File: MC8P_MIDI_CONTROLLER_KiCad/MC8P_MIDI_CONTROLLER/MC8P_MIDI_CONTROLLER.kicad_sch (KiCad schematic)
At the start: 29 parts, among them J1 MIDI OUT, SW1 ASSIGN, SW2 ENTER, SW3 PREV, SW4 NEXT, U1 Teensy4.0

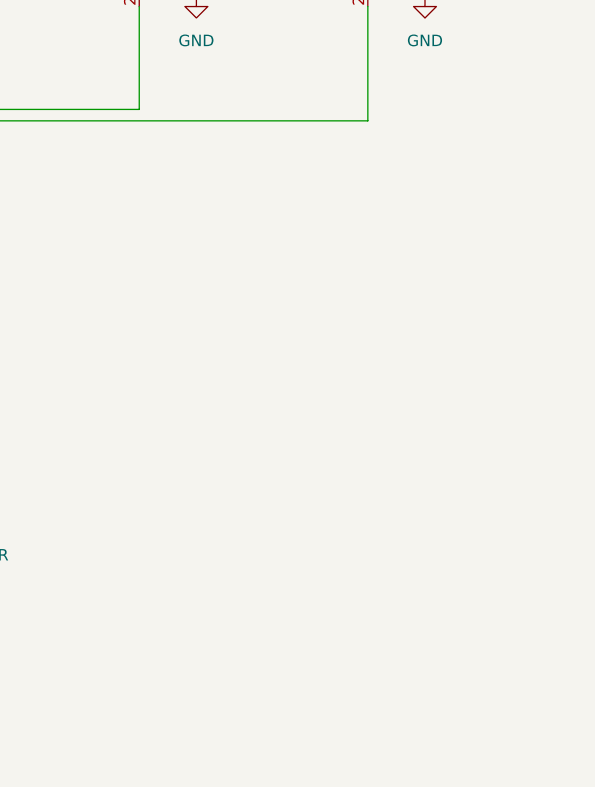
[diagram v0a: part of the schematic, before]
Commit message: Schematic update v1.2.0
- Added Bulk capacitors between the  5V and 3V3 power rails to ground for power stabilisation
- Added Decoupling capacitor between the power rails and ground for high frequency noise filtering
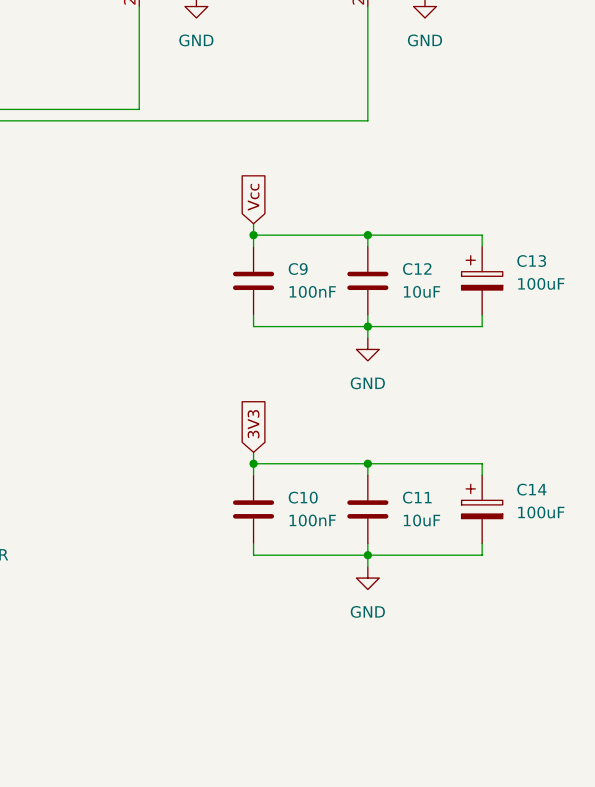
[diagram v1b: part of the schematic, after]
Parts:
- added C10, C9: 100nF, Capacitor_THT:C_Disc_D5.0mm_W2.5mm_P5.00mm, symbol Device:C
- added C11, C12: 10uF, Capacitor_THT:C_Disc_D5.0mm_W2.5mm_P5.00mm, symbol Device:C
- added C13, C14: 100uF, Capacitor_THT:CP_Radial_D4.0mm_P1.50mm, symbol Device:C_Polarized
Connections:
- net 3V3: now also C10.1, C11.1, C14.1
- net GND: now also C10.2, C11.2, C12.2, C13.2, C14.2, C9.2
- net Vcc: now also C12.1, C13.1, C9.1
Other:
- company: (none) -> .axs instruments
- title: (none) -> MC8P MIDI Controller

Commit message: PCB Update
- Fixes power resets/brownouts
- disconnected POTS, BUTTONS and MIDI OUT from Vin
- connected POTS & BUTTONS to 3V3
- connected MIDI OUT to VUSB
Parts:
- removed C10: 100nF, Capacitor_THT:C_Disc_D5.0mm_W2.5mm_P5.00mm, symbol Device:C
- removed C11: 10uF, Capacitor_THT:C_Disc_D5.0mm_W2.5mm_P5.00mm, symbol Device:C
- removed C14: 100uF, Capacitor_THT:CP_Radial_D4.0mm_P1.50mm, symbol Device:C_Polarized
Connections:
- net 3V3: now also C12.1, C13.1, C9.1, RV1.3, RV2.3, RV3.3, RV4.3, RV5.3, RV6.3, RV7.3, RV8.3, SW1.1 (A), SW2.1 (A), SW3.1 (A), SW4.1 (A)
- net Vcc: now also U1.34 (VUSB); no longer C12.1, C13.1, C9.1, RV1.3, RV2.3, RV3.3, RV4.3, RV5.3, RV6.3, RV7.3, RV8.3, SW1.1 (A), SW2.1 (A), SW3.1 (A), SW4.1 (A), U1.33 (VIN)
- no-connect marks 0 -> 33

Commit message: Schematic & PCB labelling update
Updated Capacitor labelling (C9-11)
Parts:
- renumbered C12 to C10, C13 to C11
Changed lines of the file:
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@@
 		(dnp no)
 		(fields_autoplaced yes)
-		(property "Reference" "C12"
+		(property "Reference" "C10"
 			(at 232.41 109.2199 0)
 			(effects
@@
 			(project "MC8P_MIDI_CONTROLLER"
 				(path "/42d00d8e-48e3-47e6-b456-ac5bd2d9bc78"
-					(reference "C12")
+					(reference "C10")
 					(unit 1)
 				)
@@
 		(dnp no)
 		(fields_autoplaced yes)
-		(property "Reference" "C13"
+		(property "Reference" "C11"
 			(at 245.11 108.3309 0)
 			(effects
@@
 			(project ""
 				(path "/42d00d8e-48e3-47e6-b456-ac5bd2d9bc78"
-					(reference "C13")
-					(unit 1)
-				)
+					(reference "C11")
+					(unit 1)
+				)

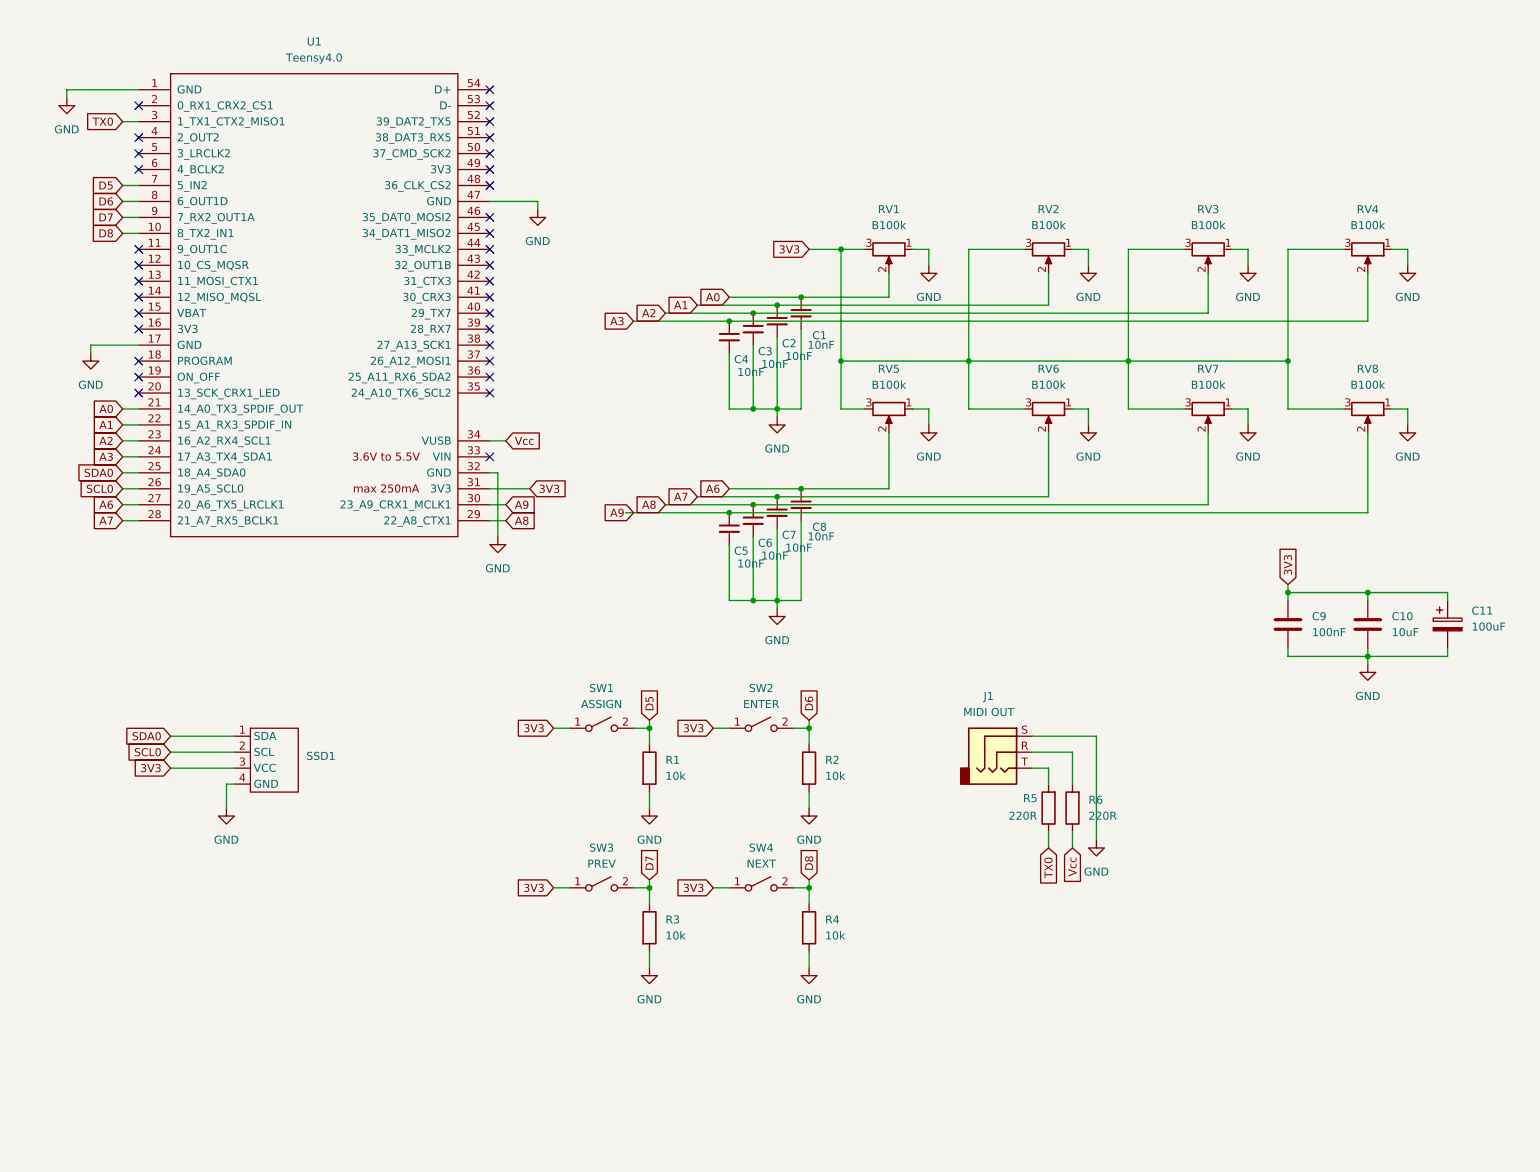
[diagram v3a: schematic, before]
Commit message: PCB Updates
- Added dedicated 5V Centre Positive power input
- Added PCBWay logo for sponsor
- Updated UI Components with new Alagard font
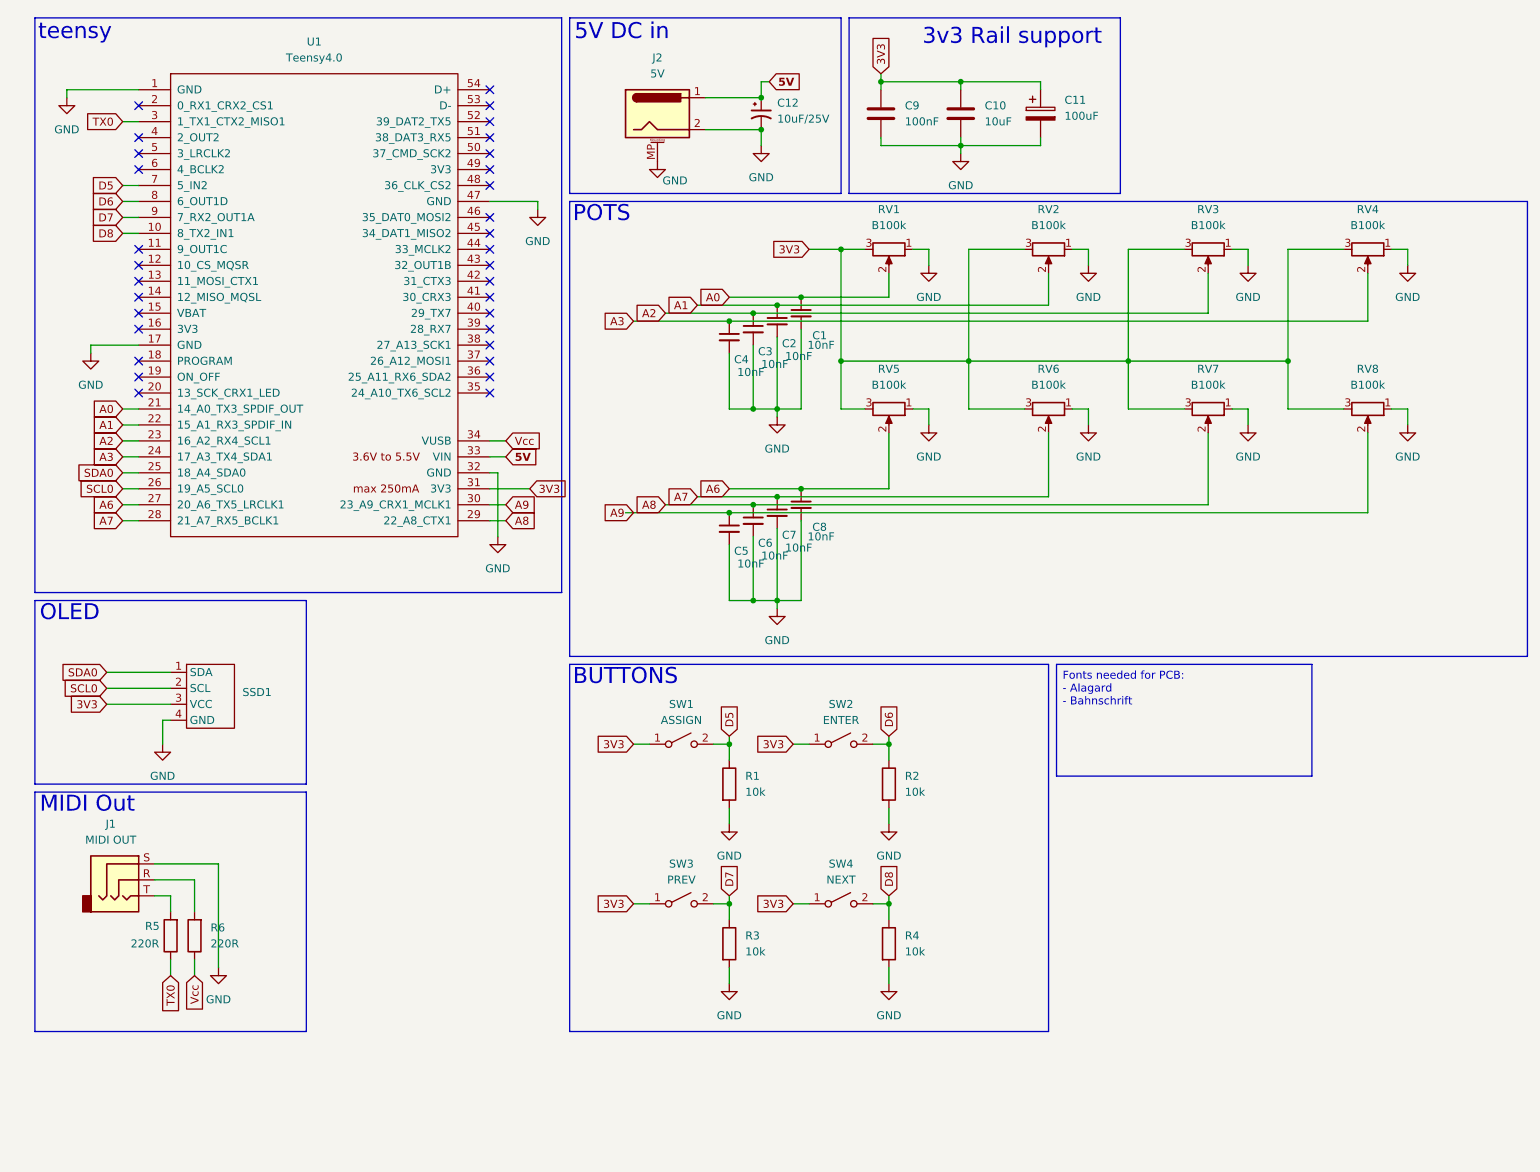
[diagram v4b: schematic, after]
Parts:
- added C12: 10uF_4x5.3_10V, Capacitor_THT:CP_Radial_D4.0mm_P1.50mm, symbol PCM_4ms_Capacitor:10uF_4x5.3_10V
- added J2: 5V, Connector_BarrelJack:BarrelJack_GCT_DCJ200-10-A_Horizontal, symbol Connector:Barrel_Jack_MountingPin
- R1, R2, R3, R4: value 10k_0402 -> 10k
- R5, R6: value 10k_0402 -> 220R
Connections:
- net GND: now also C12.2, J2.2, J2.MP (MountPin)
- net 5V: now reaches U1.33 (VIN)
- net 5V: now also C12.1, J2.1
- no-connect marks 33 -> 32
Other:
- note added: "3v3 Rail support"
- note added: "5V DC in"
- note added: "BUTTONS"
- note added: "MIDI Out"
- note added: "OLED"
- note added: "POTS"
- note added: "teensy"
- moved on the sheet: C10, C11, C9, J1, R1, R2, R3, R4, R5, R6, SSD1, SW1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

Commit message: PCB Rev3
- STM32F411CEU6 Black Pill with
W25Q64 flash
- Added DC Jack for powering externally
- restructured KiCad Folder
- Added production folder with BOM
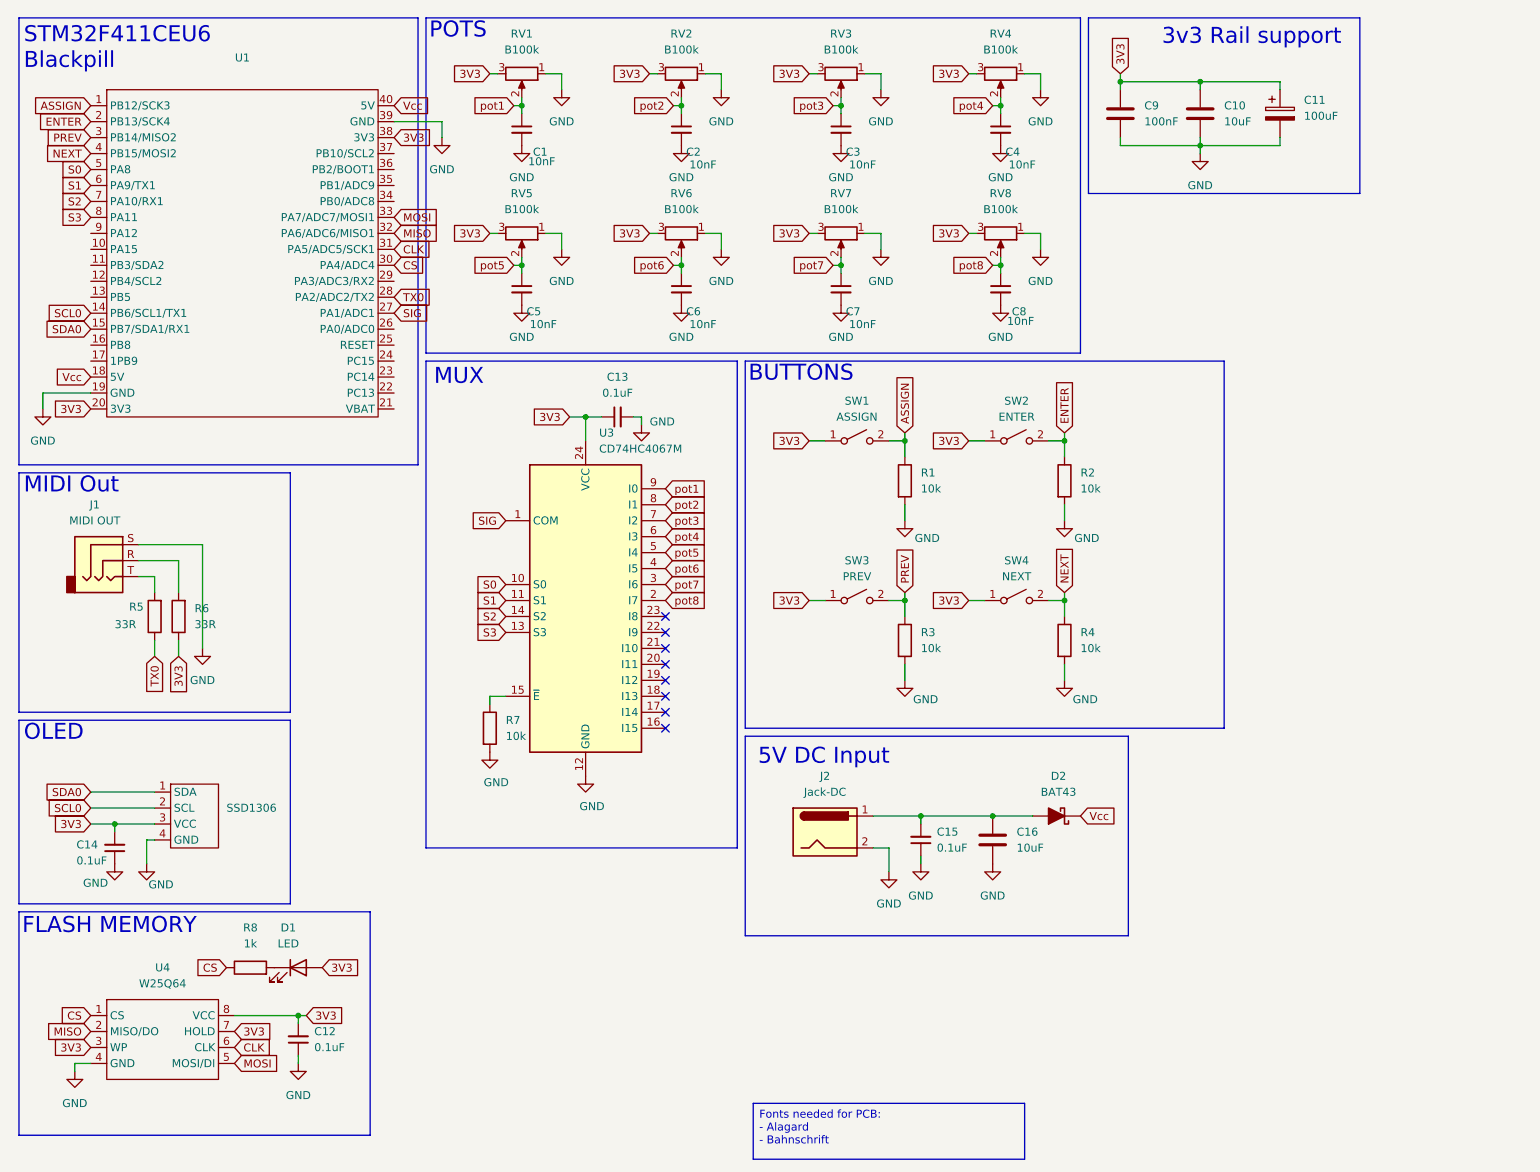
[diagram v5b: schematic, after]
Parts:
- removed C12: 10uF_4x5.3_10V, Capacitor_THT:CP_Radial_D4.0mm_P1.50mm, symbol PCM_4ms_Capacitor:10uF_4x5.3_10V
- removed J2: 5V, Connector_BarrelJack:BarrelJack_GCT_DCJ200-10-A_Horizontal, symbol Connector:Barrel_Jack_MountingPin
- removed U1: Teensy4.0, teensy:Teensy40, symbol teensy:Teensy4.0
- added C12, C13, C14, C15: 100nF_0603_16V, Capacitor_SMD:C_1206_3216Metric, symbol PCM_4ms_Capacitor:100nF_0603_16V
- added C16: 10uF, Capacitor_SMD:C_1206_3216Metric_Pad1.33x1.80mm_HandSolder, symbol Device:C
- added D1: LED, LED_SMD:LED_1206_3216Metric_Pad1.42x1.75mm_HandSolder, symbol Device:LED
- added D2: BAT43, PCM_Diode_SMD_AKL:D_1206_3216Metric_Pad1.42x1.75mm_HandSolder, symbol PCM_Diode_Schottky_AKL:BAT43
- added J2: Jack-DC, Connector_BarrelJack:BarrelJack_GCT_DCJ200-10-A_Horizontal, symbol Connector:Jack-DC
- added R7, R8: 10k_0402, PCM_4ms_Resistor:R_0603, symbol PCM_4ms_Resistor:10k_0402
- added U1: ~, blackpill:Z_module_black_pill_STM32F411, symbol STM32F411CEU6_BlackPill:BlackPill_STM32F411CEU6
- added U3: CD74HC4067M, Package_SO:SOIC-24W_7.5x15.4mm_P1.27mm, symbol 74xx:CD74HC4067M
- added U4: W25Q64, Package_SO:SOIC-8_3.9x4.9mm_P1.27mm, symbol W25Q64_SPI_FLASH:W25Q64
- C1, C2, C3, C4, C5, C6, C7, C8: footprint Capacitor_THT:C_Axial_L3.8mm_D2.6mm_P7.50mm_Horizontal -> Capacitor_SMD:C_1206_3216Metric_Pad1.33x1.80mm_HandSolder
- C10, C9: footprint Capacitor_THT:C_Disc_D5.0mm_W2.5mm_P5.00mm -> Capacitor_SMD:C_1206_3216Metric_Pad1.33x1.80mm_HandSolder
- R1, R2, R3, R4: footprint PCM_4ms_Resistor:R_Axial_DIN0207_L6.3mm_D2.5mm_P7.62mm_Horizontal -> PCM_4ms_Resistor:R_0603
- R5, R6: footprint PCM_4ms_Resistor:R_Axial_DIN0207_L6.3mm_D2.5mm_P7.62mm_Horizontal -> PCM_4ms_Resistor:R_0603; Display 220R -> 33R
- renumbered SSD1 to SSD1306
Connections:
- net 3V3: now also R6.1, C12.2, C13.1, C14.2, D1.2 (A), U1.20 (3V3), U1.38 (3V3), U3.24 (VCC), U4.3 (WP), U4.7 (HOLD), U4.8 (VCC)
- net GND: now also C12.1, C13.2, C14.1, C15.1, C16.2, J2.2, R7.2, U1.19 (GND), U1.39 (GND), U3.12 (GND), U4.4 (GND)
- net SCL0: now also U1.14 (PB6/SCL1/TX1)
- net SDA0: now also U1.15 (PB7/SDA1/RX1)
- net TX0: now also U1.28 (PA2/ADC2/TX2)
- net Vcc: now also D2.1 (K), U1.18 (5V), U1.40 (5V); no longer R6.1
- net A0 renamed pot1
- net pot1: now also U3.9 (I0)
- net A1 renamed pot2
- net pot2: now also U3.8 (I1)
- net A2 renamed pot3
- net pot3: now also U3.7 (I2)
- net A3 renamed pot4
- net pot4: now also U3.6 (I3)
- net A6 renamed pot5
- net pot5: now also C5.1, U3.5 (I4); no longer C8.1
- net A7 renamed pot6
- net pot6: now also C6.1, U3.4 (I5); no longer C7.1
- net A8 renamed pot7
- net pot7: now also C7.1, U3.3 (I6); no longer C6.1
- net A9 renamed pot8
- net pot8: now also C8.1, U3.2 (I7); no longer C5.1
- net D5 renamed ASSIGN
- net ASSIGN: now also U1.1 (PB12/SCK3)
- net D6 renamed ENTER
- net ENTER: now also U1.2 (PB13/SCK4)
- net D7 renamed PREV
- net PREV: now also U1.3 (PB14/MISO2)
- net D8 renamed NEXT
- net NEXT: now also U1.4 (PB15/MOSI2)
- new net: R7.1, U3.15 (~{E})
- new net: C15.2, C16.1, D2.2 (A), J2.1
- new net: D1.1 (K), R8.2
- new net CLK: U1.31 (PA5/ADC5/SCK1), U4.6 (CLK)
- new net CS: R8.1, U1.30 (PA4/ADC4), U4.1 (CS)
- new net MISO: U1.32 (PA6/ADC6/MISO1), U4.2 (MISO/DO)
- new net MOSI: U1.33 (PA7/ADC7/MOSI1), U4.5 (MOSI/DI)
- new net S0: U1.5 (PA8), U3.10 (S0)
- new net S1: U1.6 (PA9/TX1), U3.11 (S1)
- new net S2: U1.7 (PA10/RX1), U3.14 (S2)
- new net S3: U1.8 (PA11), U3.13 (S3)
- new net SIG: U1.27 (PA1/ADC1), U3.1 (COM)
- no-connect marks 32 -> 8
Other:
- note added: "5V DC Input"
- note added: "FLASH MEMORY"
- note added: "MUX"
- note added: "STM32F411CEU6 Blackpill"
- note removed: "5V DC in"
- note removed: "teensy"
- moved on the sheet: C1, C10, C11, C2, C3, C4, C5, C6, C7, C8, C9, J1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

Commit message: PCB revisions
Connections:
- net S3: now also U1.10 (PA15); no longer U1.8 (PA11)
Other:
- moved on the sheet: C1, C10, C11, C13, C15, C16, C2, C3, C4, C5, C6, C7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

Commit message: pcb revisions
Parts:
- D2: footprint PCM_Diode_SMD_AKL:D_1206_3216Metric_Pad1.42x1.75mm_HandSolder -> Diode_SMD:D_SOD-123
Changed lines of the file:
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@@
 		(on_board yes)
 		(dnp no)
-		(fields_autoplaced yes)
 		(property "Reference" "D2"
 			(at 183.1975 134.62 0)
@@
 			)
 		)
-		(property "Footprint" "PCM_Diode_SMD_AKL:D_1206_3216Metric_Pad1.42x1.75mm_HandSolder"
-			(at 182.88 140.97 0)
+		(property "Footprint" "Diode_SMD:D_SOD-123"
+			(at 183.388 131.572 0)
 			(effects
 				(font
